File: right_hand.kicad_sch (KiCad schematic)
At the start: 1 part

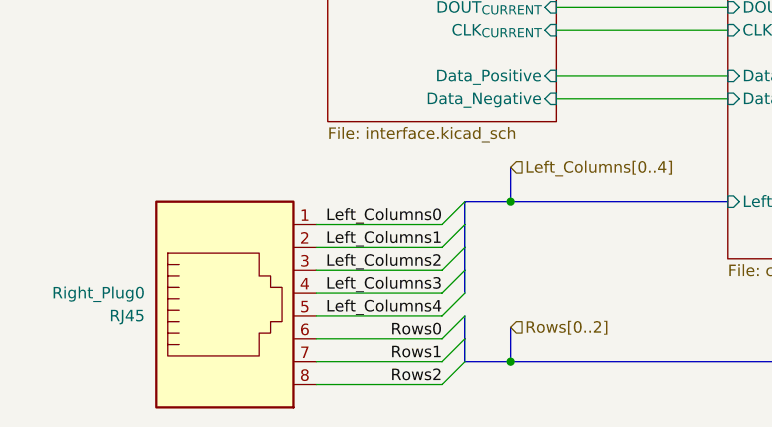
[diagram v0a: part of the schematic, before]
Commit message: Match left hand pins
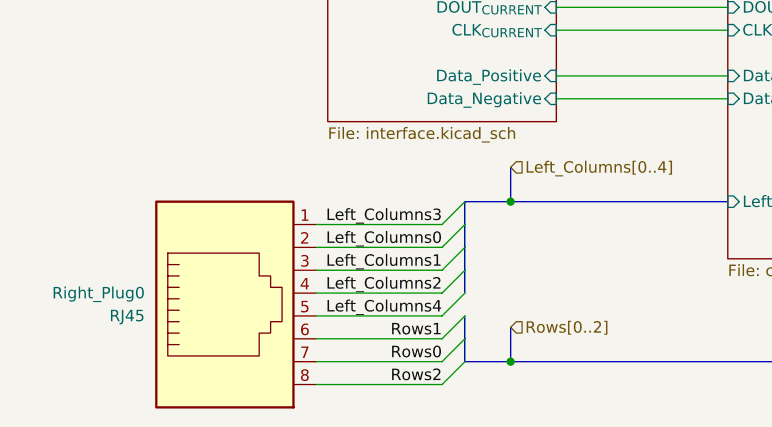
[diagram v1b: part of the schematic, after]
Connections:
- net Left_Columns0: now also Right_Plug0.2; no longer Right_Plug0.1
- net Left_Columns1: now also Right_Plug0.3; no longer Right_Plug0.2
- net Left_Columns2: now also Right_Plug0.4; no longer Right_Plug0.3
- net Left_Columns3: now also Right_Plug0.1; no longer Right_Plug0.4
- net Rows0: now also Right_Plug0.7; no longer Right_Plug0.6
- net Rows1: now also Right_Plug0.6; no longer Right_Plug0.7
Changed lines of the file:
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@@
 		)
 	)
-	(label "Left_Columns2"
+	(label "Left_Columns1"
 		(at 60.96 91.44 180)
 		(effects
@@
 		)
 	)
-	(label "Rows0"
+	(label "Rows1"
 		(at 60.96 99.06 180)
 		(effects
@@
 		)
 	)
-	(label "Left_Columns1"
+	(label "Left_Columns0"
 		(at 60.96 88.9 180)
 		(effects
@@
 		)
 	)
-	(label "Left_Columns3"
+	(label "Left_Columns2"
 		(at 60.96 93.98 180)
 		(effects
@@
 		)
 	)
-	(label "Left_Columns0"
+	(label "Left_Columns3"
 		(at 60.96 86.36 180)
 		(effects
@@
 		)
 	)
-	(label "Rows1"
+	(label "Rows0"
 		(at 60.96 101.6 180)
 		(effects

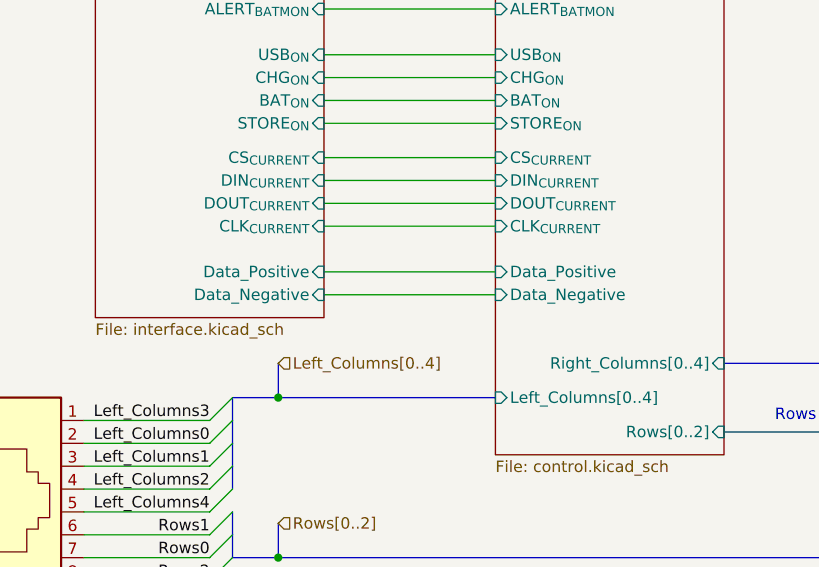
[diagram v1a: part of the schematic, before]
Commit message: Complete most of RHS layout
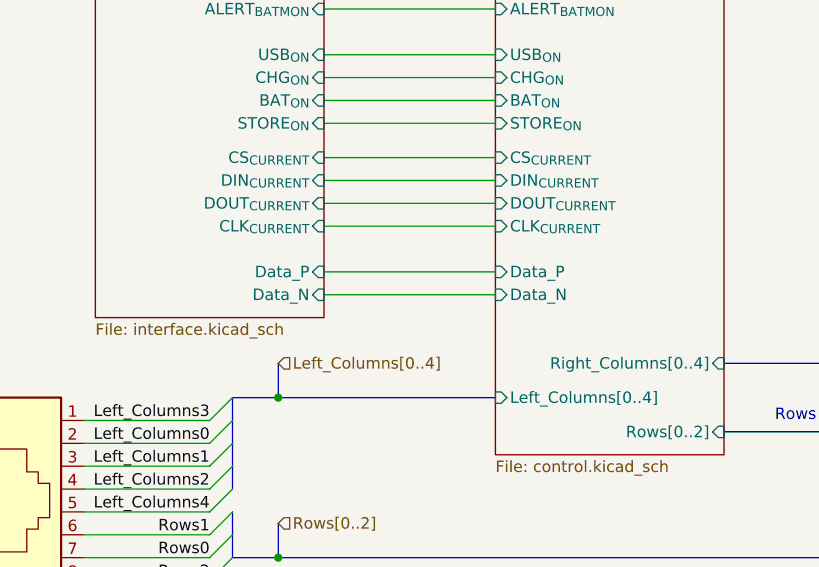
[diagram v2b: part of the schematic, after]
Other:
- sheet Control ports: added Data_N, Data_P; removed Data_Negative, Data_Positive
- sheet Interface ports: added Data_N, Data_P; removed Data_Negative, Data_Positive
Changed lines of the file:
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@@
 			)
 		)
-		(pin "Data_Negative" input
+		(pin "Data_N" input
 			(at 92.71 72.39 180)
 			(effects
@@
 			)
 		)
-		(pin "Data_Positive" input
+		(pin "Data_P" input
 			(at 92.71 69.85 180)
 			(effects
@@
 			)
 		)
-		(pin "Data_Negative" input
+		(pin "Data_N" input
 			(at 73.66 72.39 0)
 			(effects
@@
 			)
 		)
-		(pin "Data_Positive" input
+		(pin "Data_P" input
 			(at 73.66 69.85 0)
 			(effects

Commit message: Rework right hand
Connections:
- net Left_Columns0: now also Right_Plug0.4; no longer Right_Plug0.2
- net Left_Columns2: now also Right_Plug0.2; no longer Right_Plug0.4
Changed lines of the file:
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@@
 		)
 	)
-	(label "Left_Columns0"
+	(label "Left_Columns2"
 		(at 60.96 88.9 180)
 		(effects
@@
 		)
 	)
-	(label "Left_Columns2"
+	(label "Left_Columns0"
 		(at 60.96 93.98 180)
 		(effects
